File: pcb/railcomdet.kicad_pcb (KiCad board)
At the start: 4 copper layers, 110 x 70 mm, 163 parts, among them J1 MVE252-5-V, J10 MVE252-5-V, J2 MVE252-5-V, J3 MVE252-5-V, J4 MVE252-5-V, J5 MVE252-5-V, J6 PINHEADER, J7 PINHEADER, J8 PROG/DEBUG, J9 MVE252-5-V, SW1 6x6, U1 VO0631T, U10 LM339, U11 LM339, U12 STM32F103C8Tx, U13 AMS1117-3.3, U14 L78L05_SOT89, U15 SN75176AP, U2 VO0631T, U3 VO0631T, U4 L78L05_SOT89, U5 L79L05_SOT89, U6 LM339, U7 LM339, U8 LM339, U9 4052, Y1 14,7456MHz

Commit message: Use MAX478 as a MTBbus driver.
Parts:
- U15: value SN75176AP -> MAX487
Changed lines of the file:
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@@
         (effects (font (size 1 1) (thickness 0.15)))
     )
-    (fp_text value "SN75176AP" (at 3.81 9.95 90) (layer "F.Fab")
+    (fp_text value "MAX487" (at 3.81 9.95 90) (layer "F.Fab")
         (effects (font (size 1 1) (thickness 0.15)))
     )

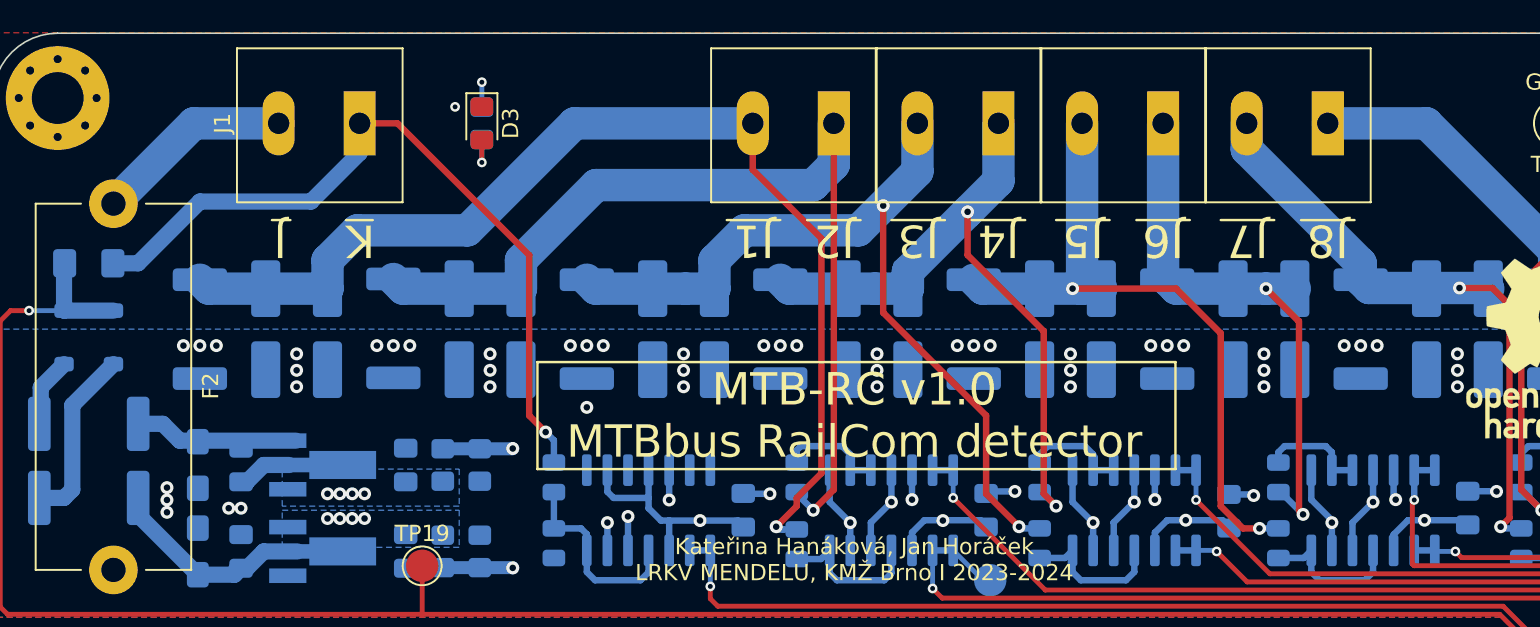
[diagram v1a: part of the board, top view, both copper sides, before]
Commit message: Use double J & K connectors.
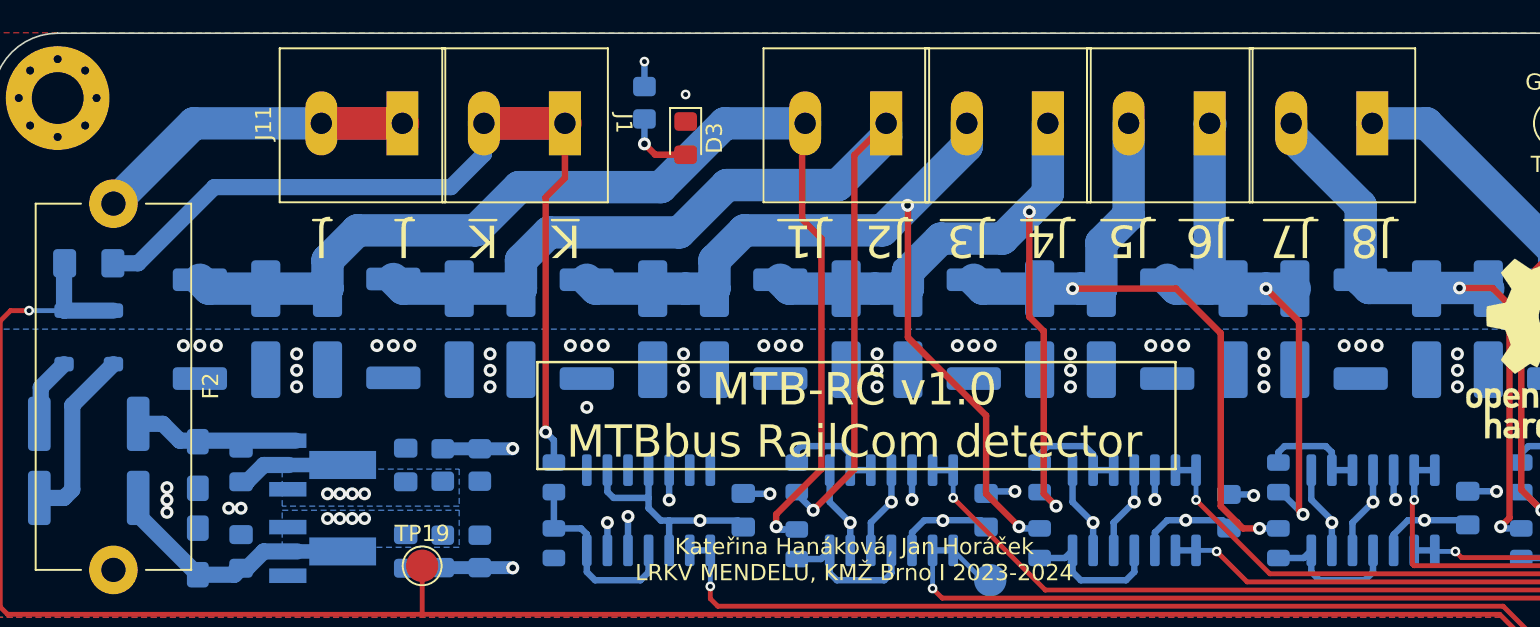
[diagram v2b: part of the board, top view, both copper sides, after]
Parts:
- added J11: MVE252-5-V, TerminalBlock_Euroclamp:MVE252-5-V, F.Cu at (122.8, 35.5)
- moved J1 12.7 mm to (132.8, 35.5)
- moved D3 12.6 mm to (142.7, 36.5)
- moved R28 10.1 mm to (140.2, 34.3)
- moved J2 3.23 mm to (152.6, 35.5)
- moved J3 3.05 mm to (162.6, 35.5)
- moved J4 2.87 mm to (172.6, 35.5)
- moved J5 2.75 mm to (182.6, 35.5)
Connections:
- J1 pad 2: /DCC/J -> K
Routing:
- net /DCC/J: track 12.2 -> 24.9 mm
- net K: track 47.1 -> 59.2 mm
- net /DCC/J2: track 60.1 -> 63.7 mm
- net /DCC/J1: track 68.7 -> 72.2 mm
- net /DCC/J8: track 46.2 -> 43.5 mm
- net /DCC/J4: track 42.4 -> 44.3 mm
- net /DCC/J3: track 52.2 -> 53.7 mm
- net Net-(D3-A): track 2.98 -> 4.36 mm
- net /DCC/J7: track 39.4 -> 38.3 mm
- net /DCC/J5: track 43.4 -> 44.1 mm
- net /DCC/J6: track 34.9 -> 35.4 mm

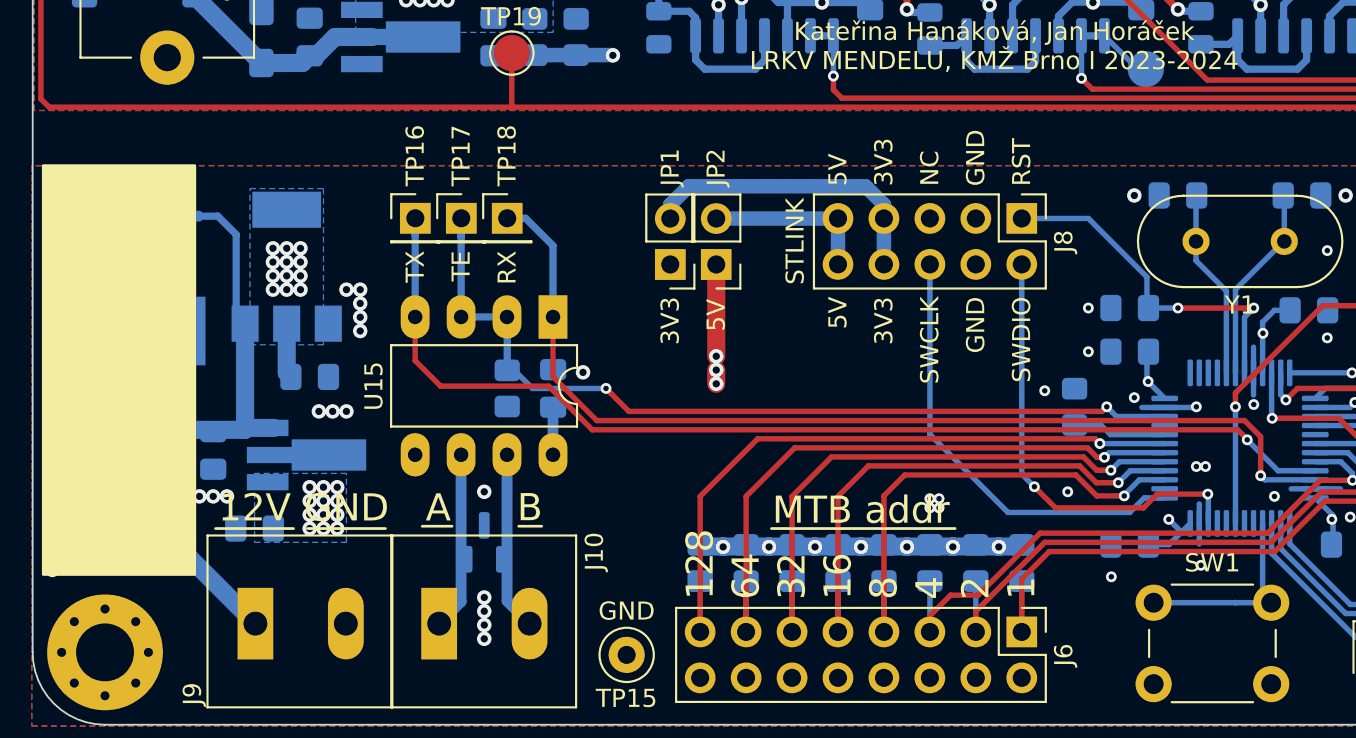
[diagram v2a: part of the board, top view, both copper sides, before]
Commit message: 78L05 -> 78M05. AMS1113-3.3 -> HT7533.
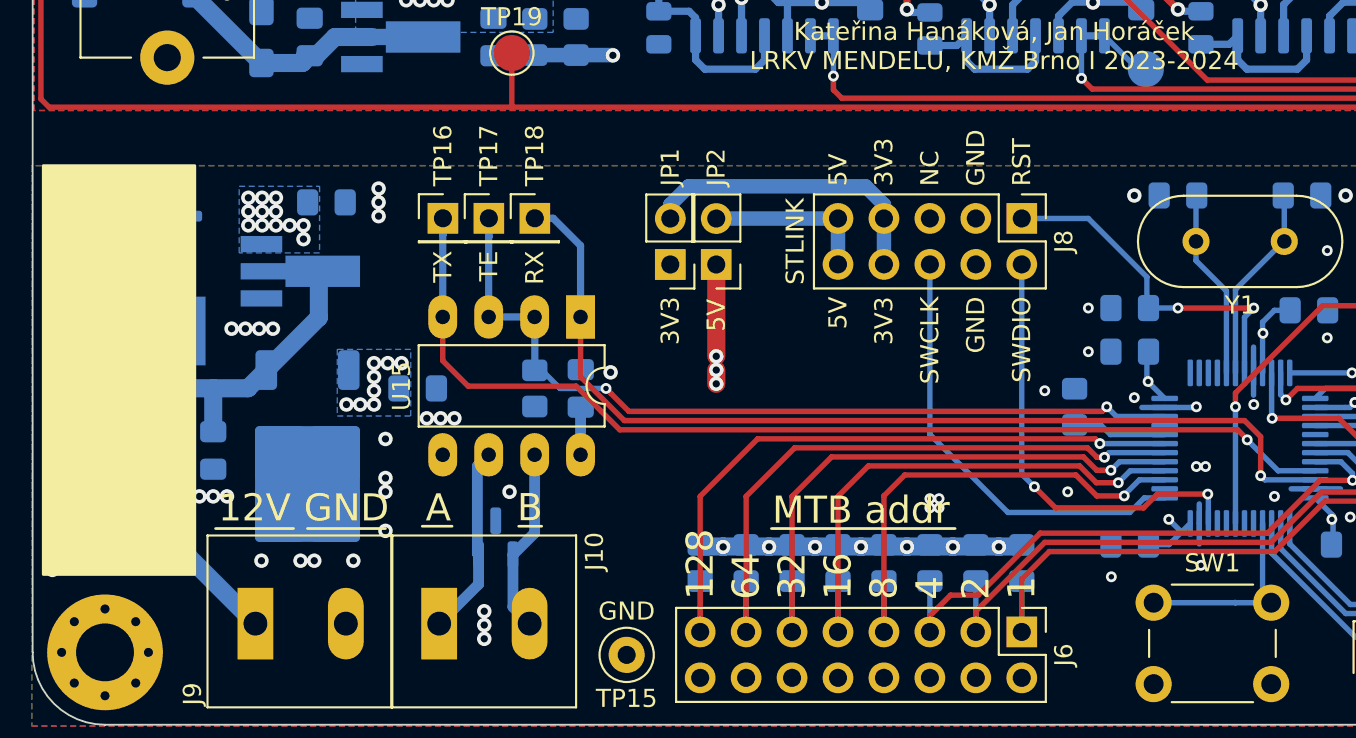
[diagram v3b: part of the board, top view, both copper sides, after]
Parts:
- U13: value AMS1117-3.3 -> HT7533-1; footprint Package_TO_SOT_SMD:SOT-223-3_TabPin2 -> Package_TO_SOT_SMD:SOT-89-3_Handsoldering
- U14: value L78L05_SOT89 -> 78M05; footprint Package_TO_SOT_SMD:SOT-89-3_Handsoldering -> Package_TO_SOT_SMD:TO-252-2
- Y1: value 14,7456MHz -> 14.7456MHz
- moved C24 11.9 mm to (121.3, 81.4), turned to 180 degrees
- moved C25 9.70 mm to (116.2, 71.1)
- moved C27 1.52 mm to (130.3, 81.4)
- moved R43 1.52 mm to (127.8, 81.4)
- moved TP16 1.52 mm to (122.7, 72.0)
- moved TP17 1.52 mm to (125.2, 72.0)
- moved TP18 1.52 mm to (127.8, 72.0)
- moved U15 1.52 mm to (130.3, 77.5)
- moved U13 1.08 mm to (115.1, 74.9), turned to 0 degrees
- moved D10 0.68 mm to (125.6, 89.7)
- moved U14 0.42 mm to (115.2, 85.4), turned to -90 degrees
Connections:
- U13 pad 2: +3V3 -> Net-(D7-A)
- U13 pad 3: Net-(D7-A) -> +3V3
- U14 pad 1: +5V -> Net-(D7-A)
- U14 pad 3: Net-(D7-A) -> +5V
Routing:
- net Net-(D7-A): track 32.9 -> 40.5 mm
- net +3V3: track 45.8 -> 42.8 mm
- net /BUS+: track 8.82 -> 10.5 mm
- net MTB-RX: track 56.2 -> 54.7 mm
- net MTB-TX: track 60.4 -> 58.9 mm
- net MTB-TE: track 49.0 -> 47.5 mm
- net /BUS-: track 8.84 -> 10.2 mm
- net +5V: track 121.8 -> 122.8 mm, vias 17 -> 13
- net GND: vias 60 -> 69
- removed copper zone on In1.Cu, net +5V

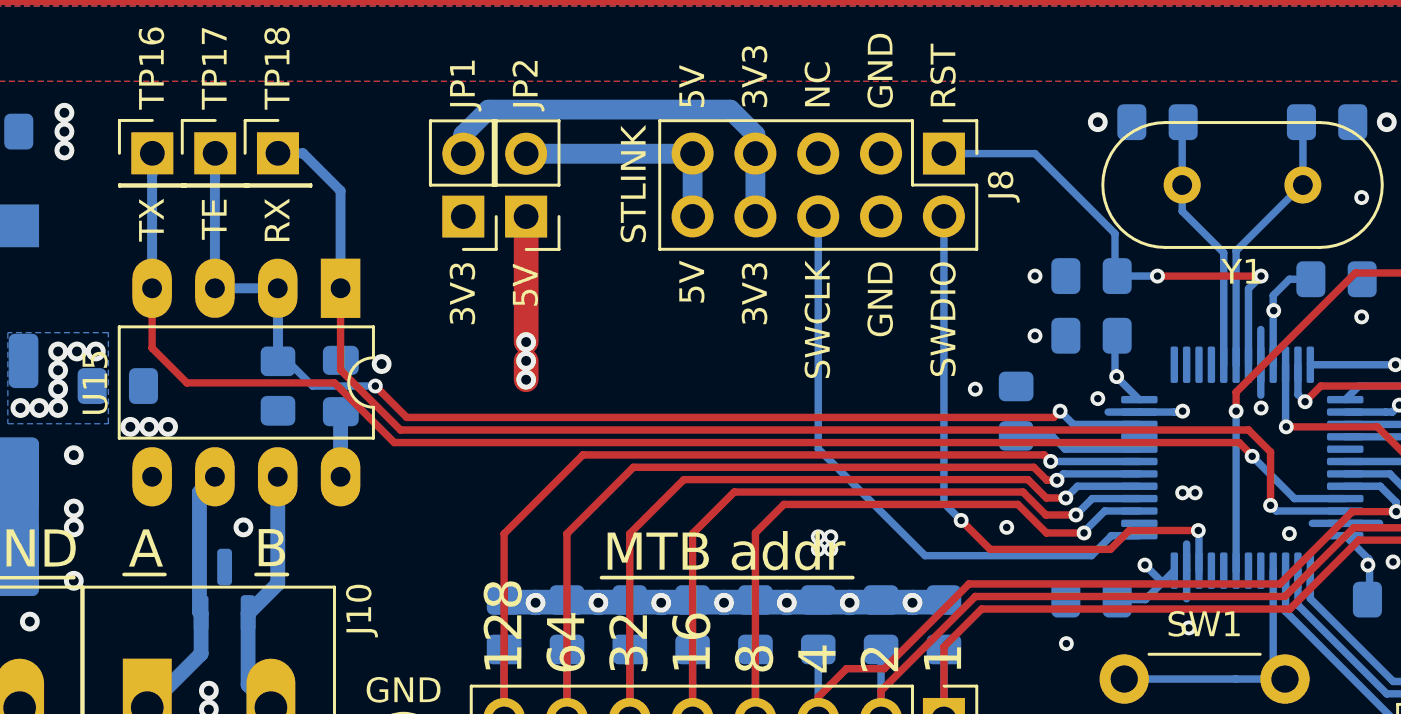
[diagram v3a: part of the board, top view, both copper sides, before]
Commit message: Add RS485 level shifting.
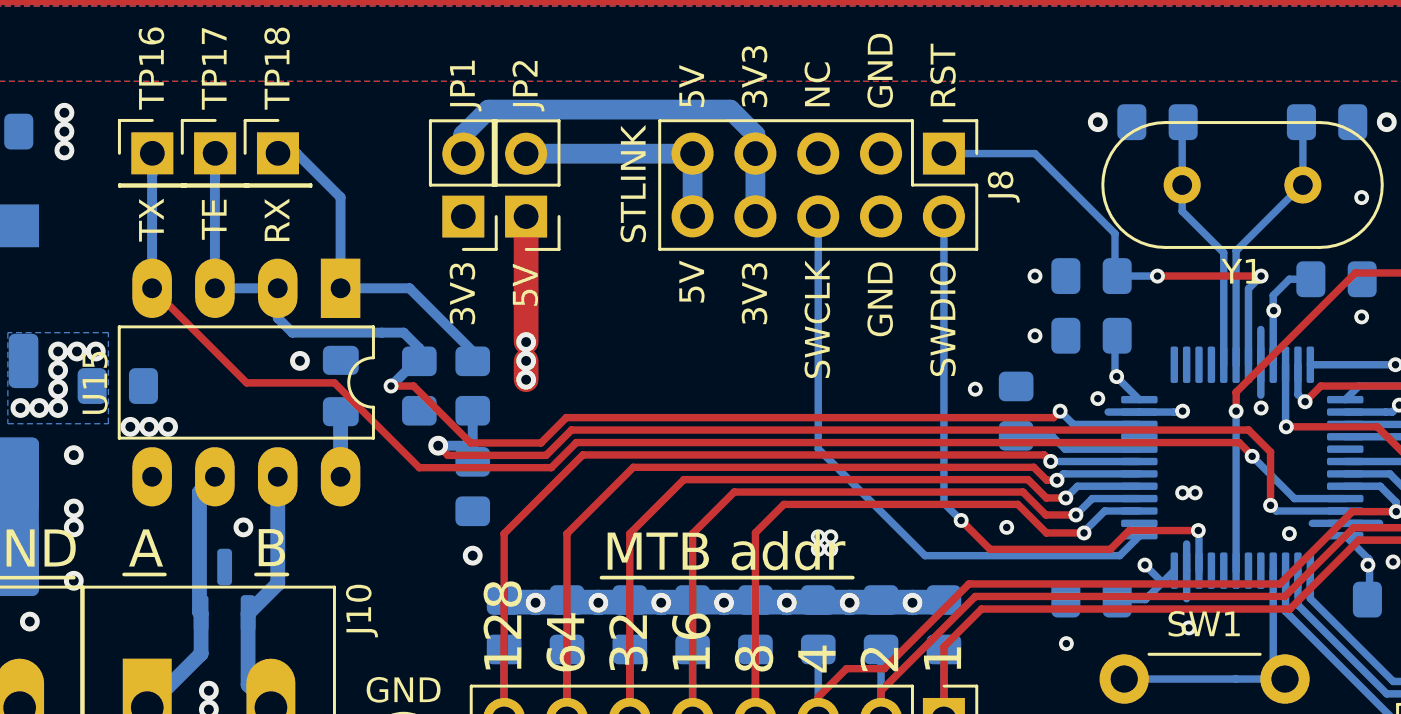
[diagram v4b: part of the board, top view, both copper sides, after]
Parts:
- added R53: 2k2, Resistor_SMD:R_0805_2012Metric_Pad1.20x1.40mm_HandSolder, B.Cu at (135.6, 81.4)
- added R54: 4k7, Resistor_SMD:R_0805_2012Metric_Pad1.20x1.40mm_HandSolder, B.Cu at (135.6, 85.5)
- moved R43 5.72 mm to (133.5, 81.4)
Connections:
- TP18 pad 1: MTB-RX -> Net-(U15-R)
- U15 pad 1: MTB-RX -> Net-(U15-R)
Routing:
- net Net-(U15-R): track 0.00 -> 13.7 mm
- net MTB-RX: track 54.7 -> 43.3 mm, vias 1 -> 2
- net MTB-TE: track 47.5 -> 49.9 mm
- net MTB-TX: track 58.9 -> 58.3 mm
- net GND: vias 69 -> 70

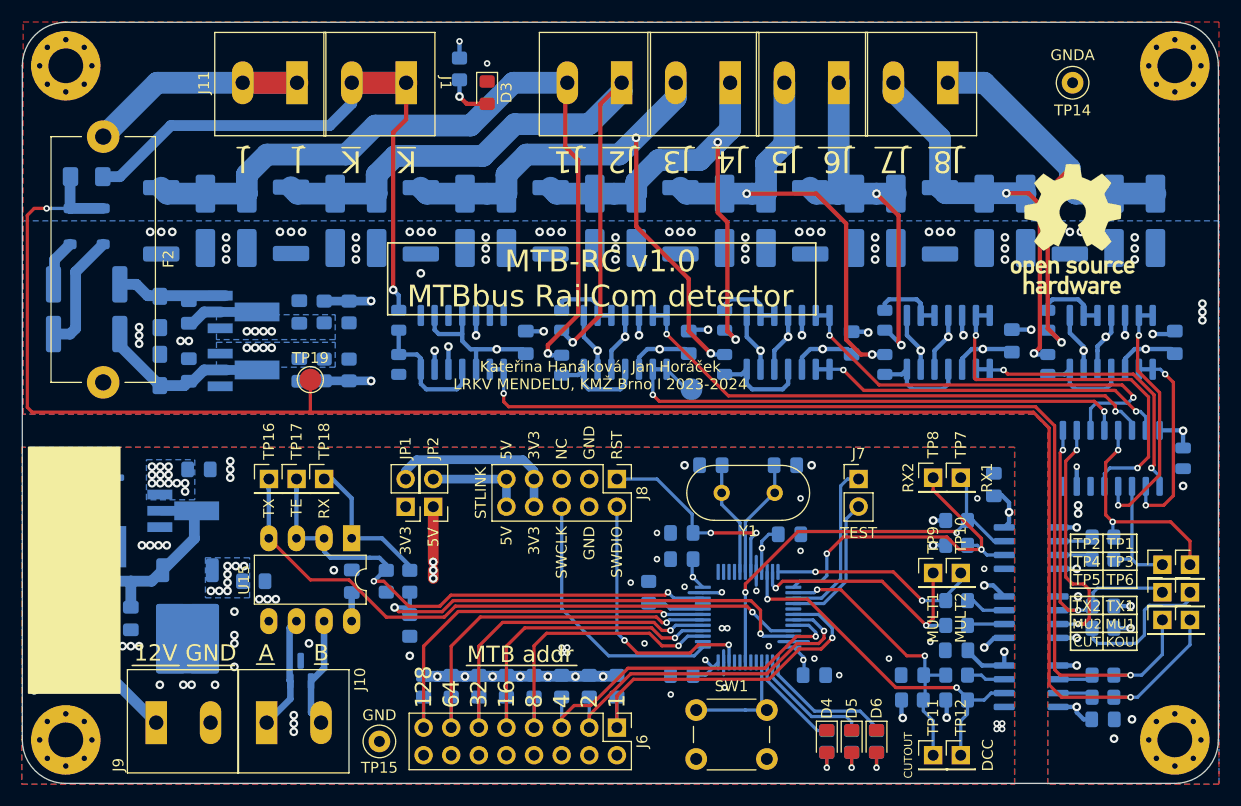
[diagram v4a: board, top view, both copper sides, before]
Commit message: Resolve some DRC issues.
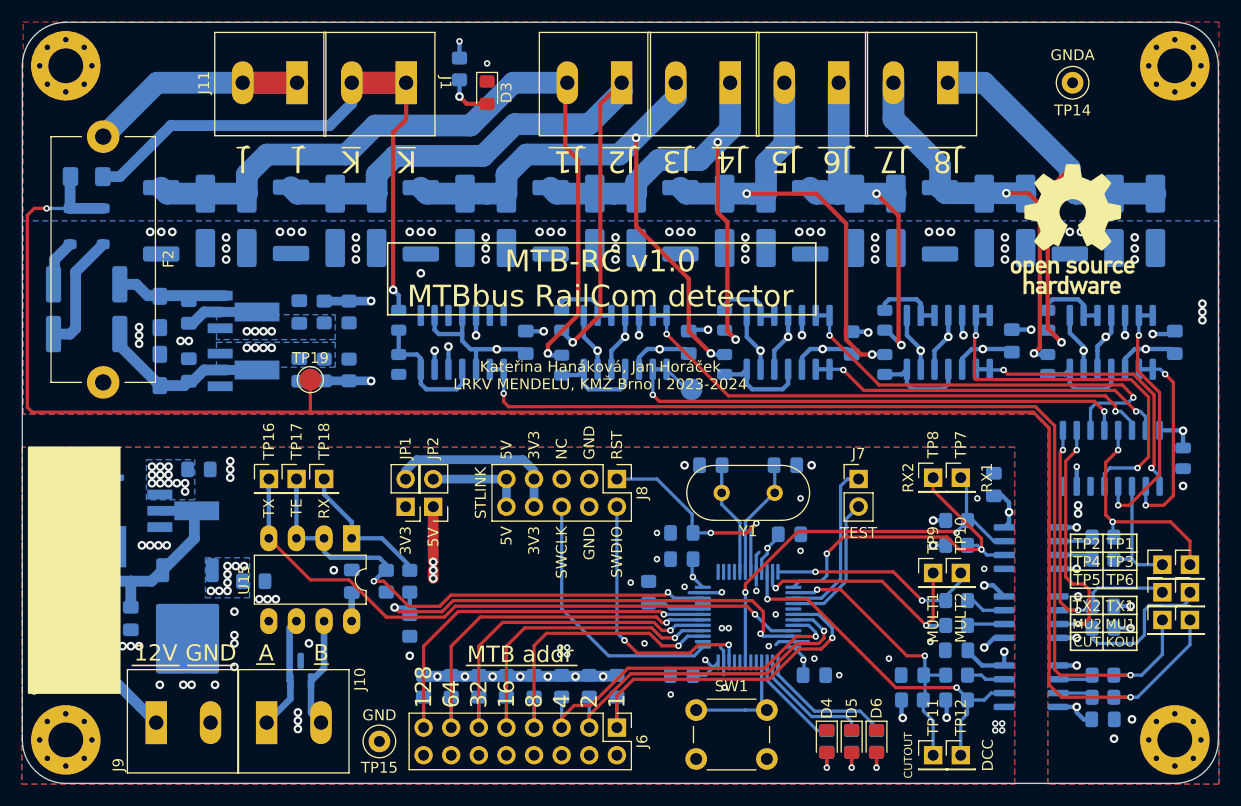
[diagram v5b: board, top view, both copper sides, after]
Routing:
- net /DCC/J1: track 72.2 -> 70.7 mm
- net GND: track 10.9 -> 12.2 mm, vias 70 -> 71
- net RST: track 19.7 -> 20.9 mm
- net Net-(D7-A): track 40.5 -> 41.5 mm
- net +3V3: track 42.8 -> 42.2 mm
